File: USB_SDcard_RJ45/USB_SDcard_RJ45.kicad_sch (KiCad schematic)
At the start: 26 parts, among them J1 HOST, J2 USB_A_Stacked, J3 USB_A_Stacked, J4 POWER, J5 RJ45_Hanrun_HR911105A_Horizon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, J6 Micro_SD_Card_Det1, U1 CH217K, U2 CH339F, Y1 25MHz

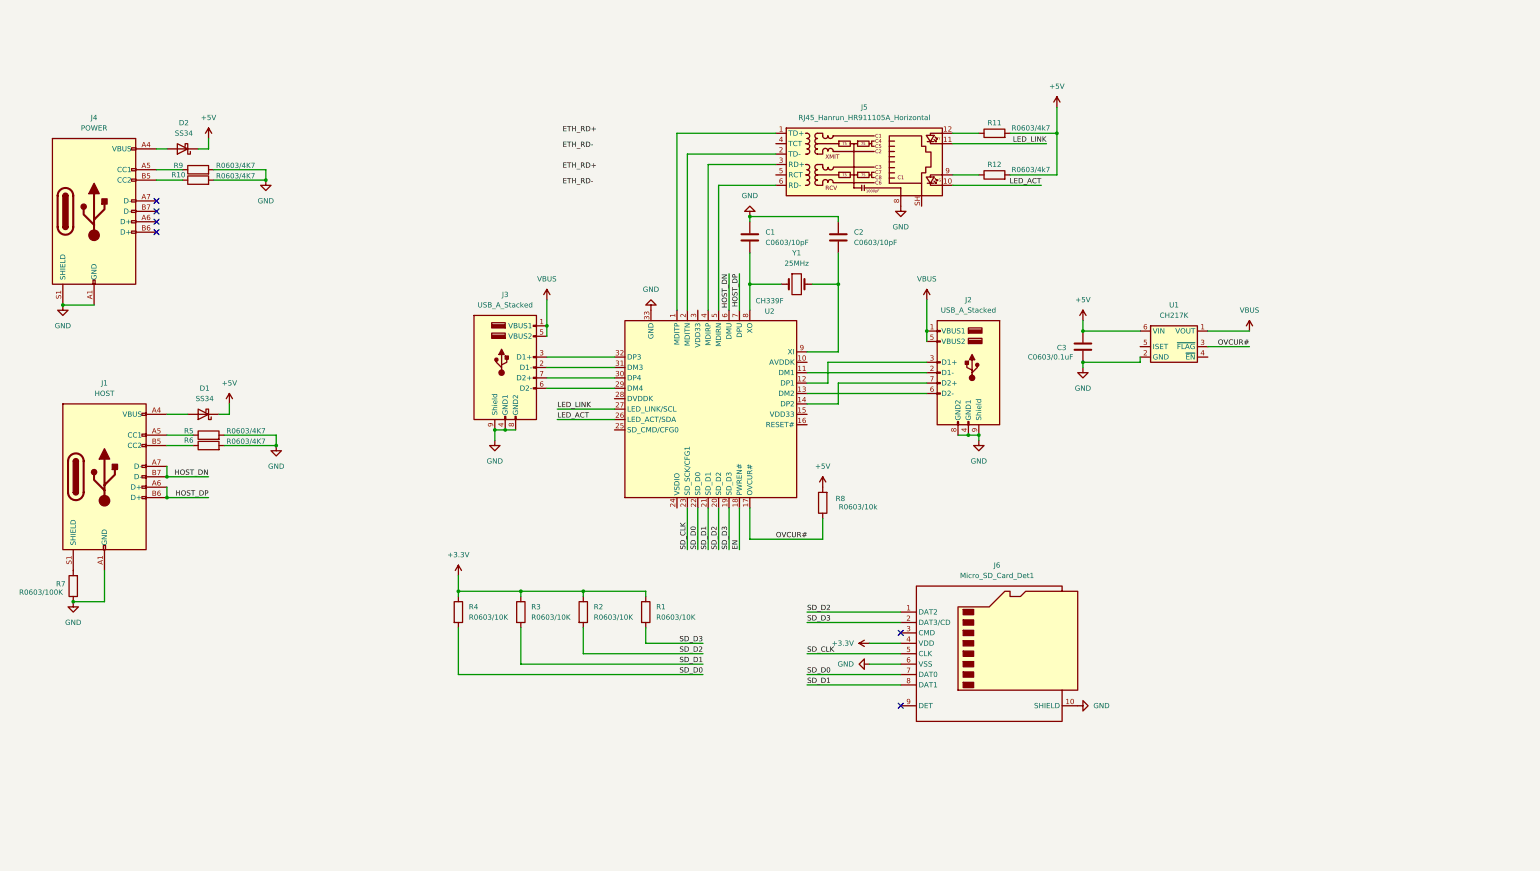
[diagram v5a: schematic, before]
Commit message: Change layout to match CH339W
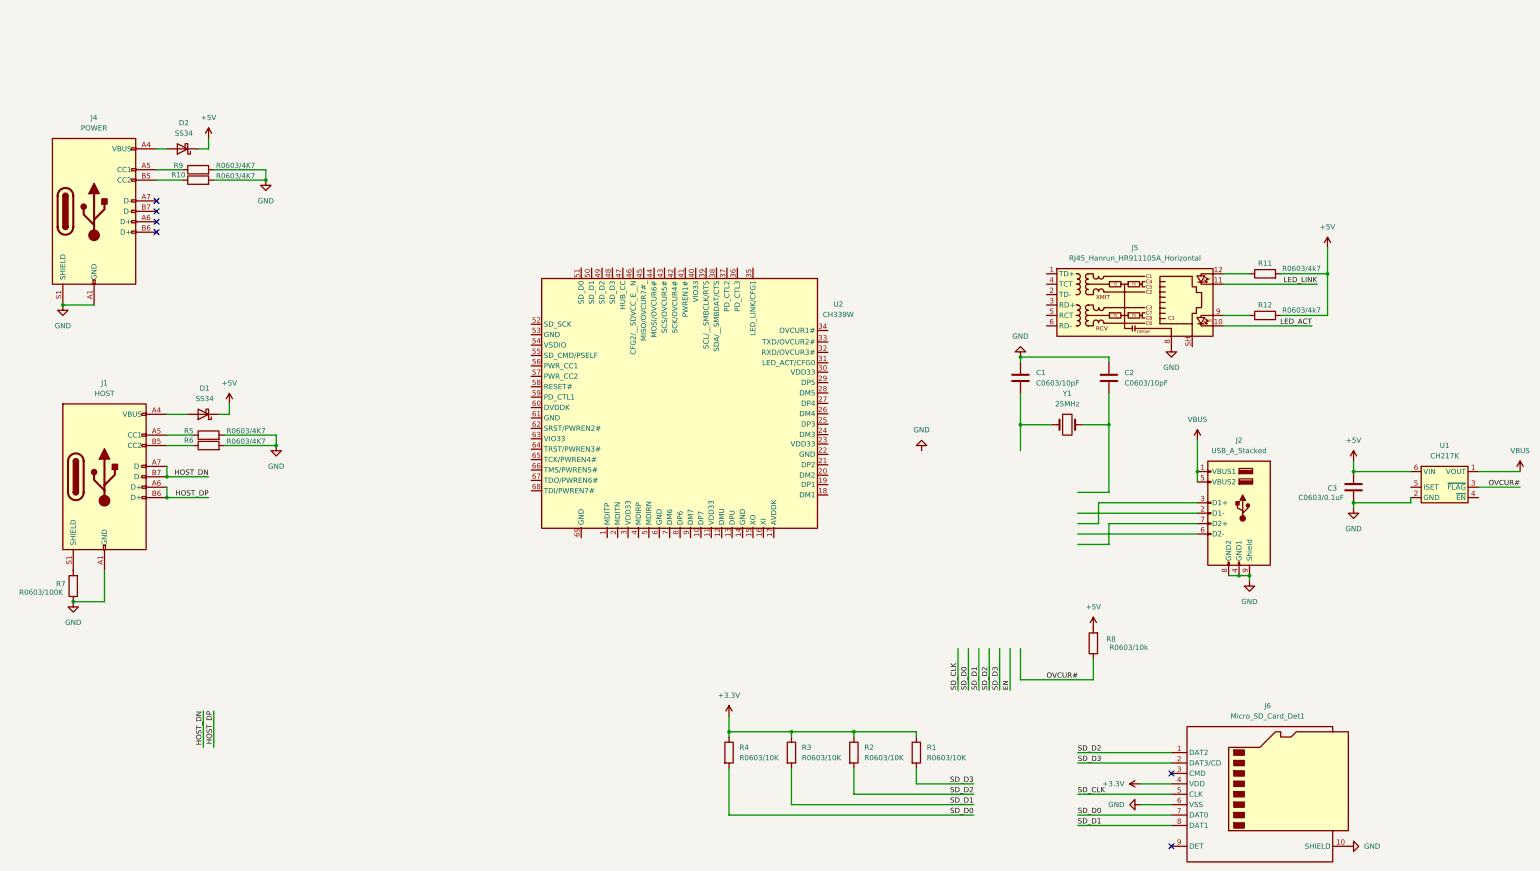
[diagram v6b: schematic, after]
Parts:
- removed J3: USB_A_Stacked, Connector_USB:USB_A_CUI_UJ2-ADH-TH_Horizontal_Stacked, symbol Connector:USB_A_Stacked
- removed U2: CH339F, Package_DFN_QFN:QFN-32-1EP_4x4mm_P0.4mm_EP2.65x2.65mm_ThermalVias, symbol 3in1lib:CH339F
- added U2: CH339W, Package_DFN_QFN:QFN-68-1EP_8x8mm_P0.4mm_EP5.2x5.2mm, symbol 3in1lib:CH339W
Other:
- moved on the sheet: C1, C2, C3, J2, J5, J6, R1, R11, R12, R2, R3, R4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

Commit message: Change USB type
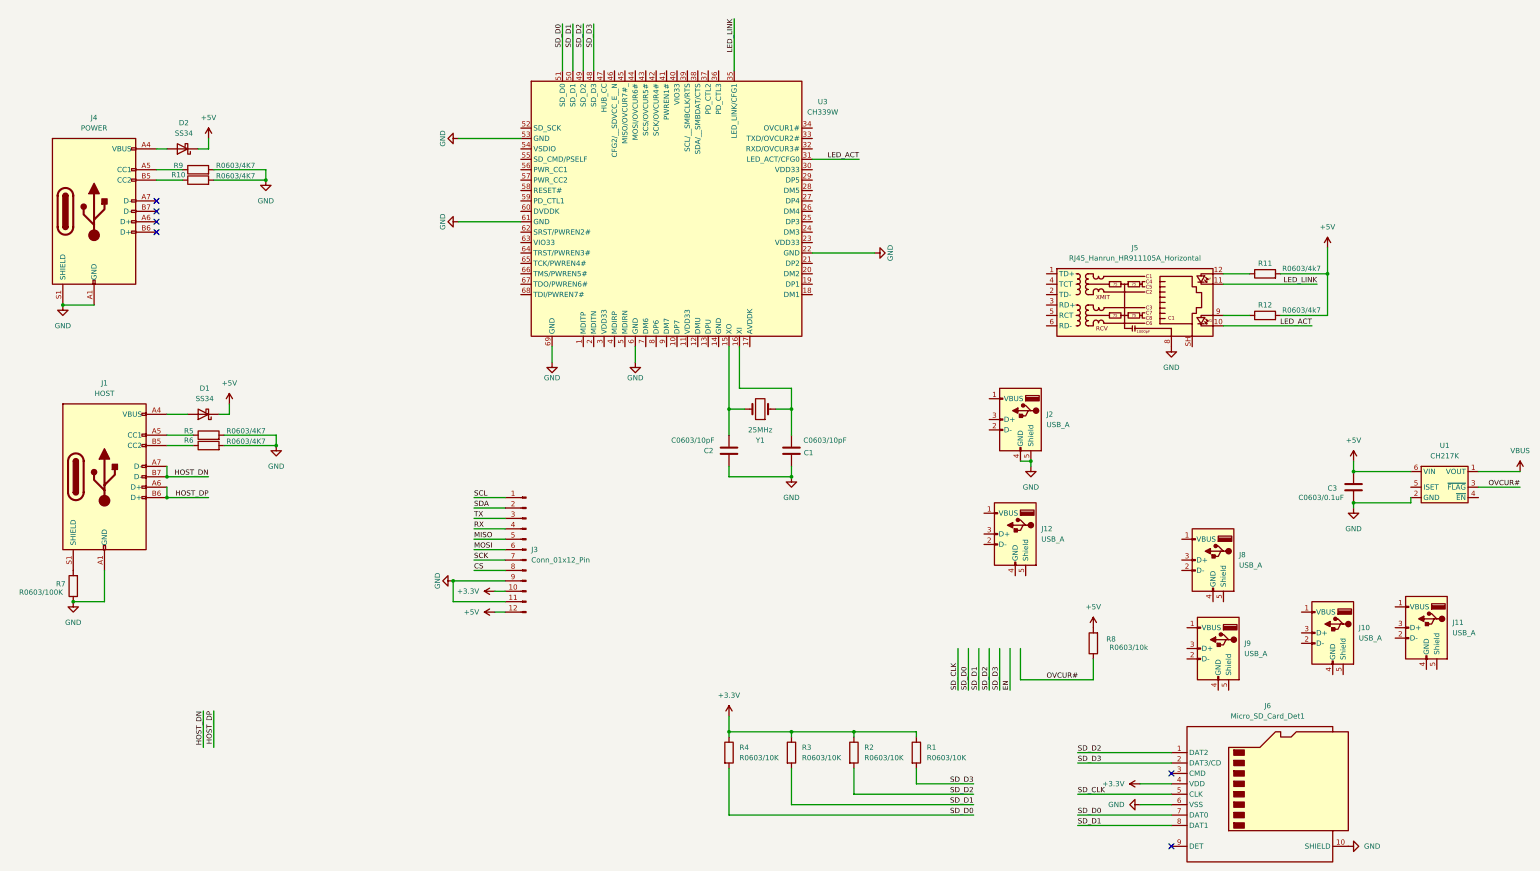
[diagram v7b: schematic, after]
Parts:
- removed J2: USB_A_Stacked, Connector_USB:USB_A_CUI_UJ2-ADH-TH_Horizontal_Stacked, symbol Connector:USB_A_Stacked
- removed U2: CH339W, Package_DFN_QFN:QFN-68-1EP_8x8mm_P0.4mm_EP5.2x5.2mm, symbol 3in1lib:CH339W
- added J10, J11, J12, J2, J8, J9: USB_A, 3in1:USB_A_Wuerth_614004134726_Horizontal, symbol Connector:USB_A
- added J3: Conn_01x12_Pin, Connector_PinHeader_2.54mm:PinHeader_1x12_P2.54mm_Horizontal, symbol Connector:Conn_01x12_Pin
- added U3: CH339W, Package_DFN_QFN:QFN-68-1EP_8x8mm_P0.4mm_EP5.2x5.2mm, symbol 3in1lib:CH339W
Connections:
- net +3.3V: now also J3.10 (Pin_10)
- net +5V: now also J3.12 (Pin_12)
- net GND: now also J2.4 (GND), J2.5 (Shield), J3.11 (Pin_11), J3.9 (Pin_9), U3.22 (GND), U3.53 (GND), U3.6 (GND), U3.61 (GND), U3.69 (GND)
- net LED_ACT: now also U3.31 (LED_ACT/CFG0)
- net LED_LINK: now also U3.35 (LED_LINK/CFG1)
- net SD_D0: now also U3.51 (SD_D0)
- net SD_D1: now also U3.50 (SD_D1)
- net SD_D2: now also U3.49 (SD_D2)
- net SD_D3: now also U3.48 (SD_D3)
- net at C2.2, Y1.2: now also U3.15 (XO)
- net at C1.2, Y1.1: now also U3.16 (XI)
- new net CS: J3.8 (Pin_8)
- new net MISO: J3.5 (Pin_5)
- new net MOSI: J3.6 (Pin_6)
- new net RX: J3.4 (Pin_4)
- new net SCK: J3.7 (Pin_7)
- new net SCL: J3.1 (Pin_1)
- new net SDA: J3.2 (Pin_2)
- new net TX: J3.3 (Pin_3)
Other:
- moved on the sheet: C1, C2, Y1
